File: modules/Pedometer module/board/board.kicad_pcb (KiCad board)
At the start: 2 copper layers, 54 parts, among them IC1 DW01A, J1 USB_C_Receptacle, J2 Conn_02x12_Odd_Even, J3 Conn_01x06_Female, J4 Conn_01x08_Female, J5 Conn_01x02_Female, Q1 AO3400A, Q2 AO3401A, Q3 FS8205A, SW1 SW_Push, SW2 SW_Push, U1 HT7833, U2 ESP32-WROOM-32D, U3 ADXL345BCCZ, U4 TP4056

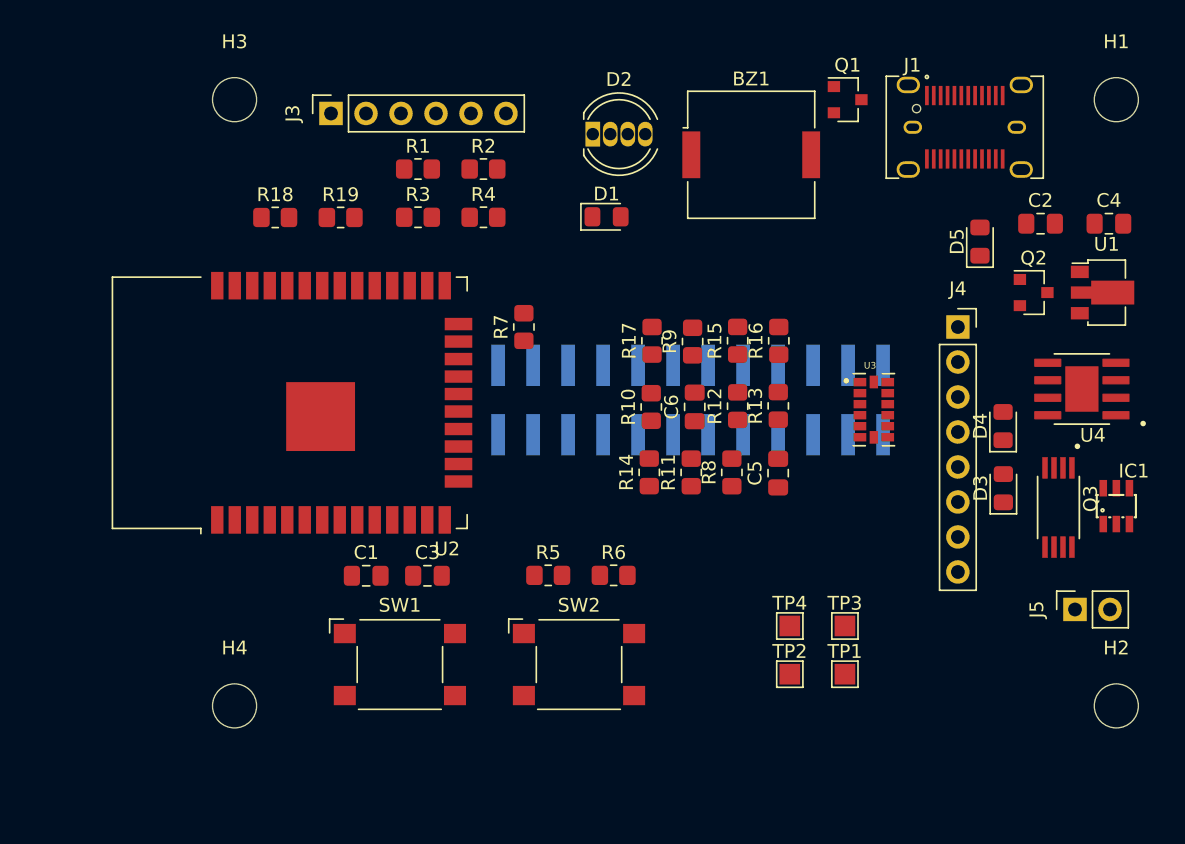
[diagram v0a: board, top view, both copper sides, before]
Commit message: Pedometer module: Schematic and PCB layout
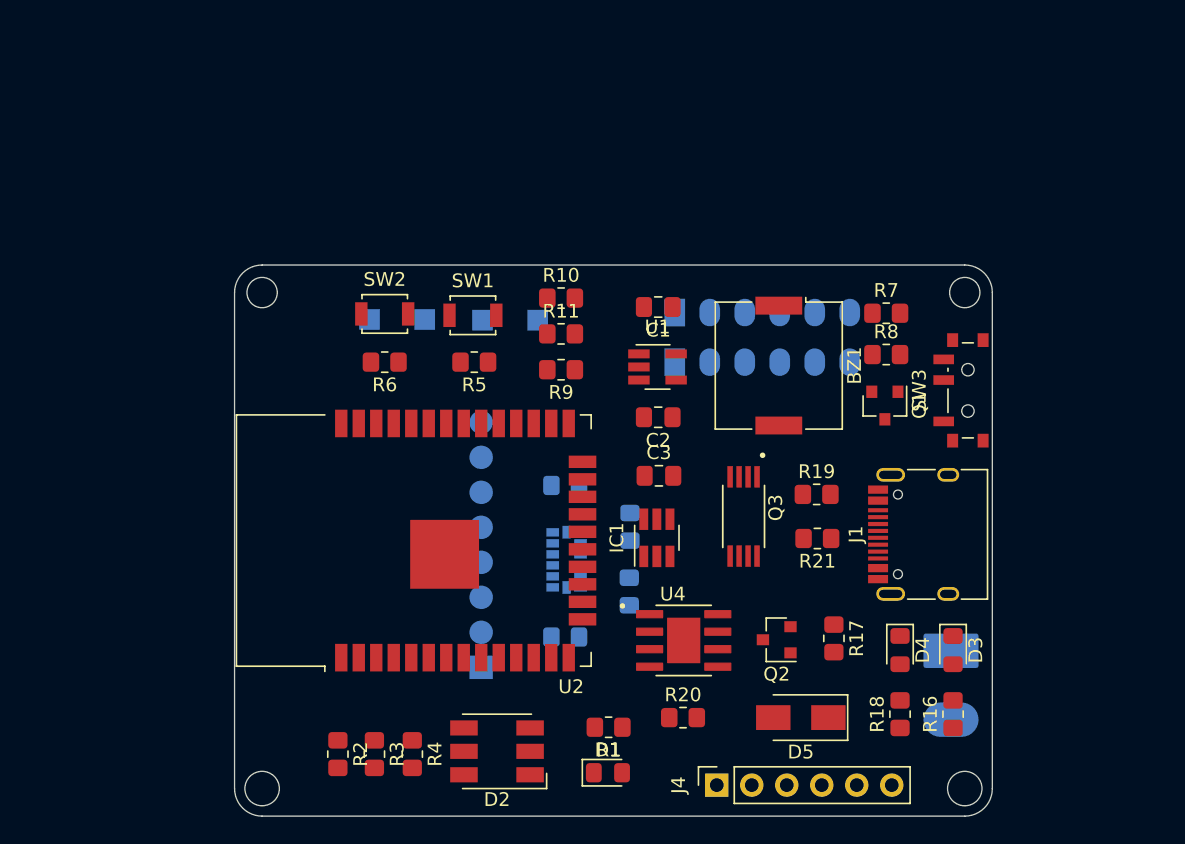
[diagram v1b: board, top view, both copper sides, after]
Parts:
- removed the C1 at (127.6, 112.6)
- removed the C3 at (132.0, 112.6)
- removed C6: 10uF, Capacitor_SMD:C_0805_2012Metric_Pad1.18x1.45mm_HandSolder
- added J3: Conn_01x06_Female, Board:SolderWire_1x06_P2.54mm, B.Cu at (149.9, 97.0)
- added R7: 100R, Resistor_SMD:R_0805_2012Metric_Pad1.20x1.40mm_HandSolder, F.Cu at (165.3, 93.5)
- added R8: 10k, Resistor_SMD:R_0805_2012Metric_Pad1.20x1.40mm_HandSolder, F.Cu at (165.3, 96.5)
- added SW3: SW_SPST, Board:SW-SPDT-PCM12, F.Cu at (170.9, 99.1)
- C1: renamed from C2; value 1uF -> 10uF
- C2: renamed from C4; value 2.2uF -> 10uF
- D2: value LED_RGBC -> LED_RGB; footprint LED_THT:LED_D5.0mm-4_RGB -> LED_SMD:LED_RGB_5050-6
- D5: footprint Diode_SMD:D_0805_2012Metric_Pad1.15x1.40mm_HandSolder -> Diode_SMD:D_SMA
- H1, H2: footprint MountingHole:MountingHole_3.2mm_M3 -> MountingHole:MountingHole_2.2mm_M2
- H3, H4: footprint MountingHole:MountingHole_3.2mm_M3 -> MountingHole:MountingHole_2.5mm
- IC1: footprint board:SOT23-6 -> Package_TO_SOT_SMD:SOT-23-6_Handsoldering
- J1: value USB_C_Receptacle -> USB_C_Receptacle_USB2.0; footprint Connector_USB:USB_C_Receptacle_JAE_DX07S024WJ1R350 -> Connector_USB:USB_C_Receptacle_HRO_TYPE-C-31-M-12
- J2: value Conn_02x12_Odd_Even -> Conn_01x06_Female; footprint Connector_PinSocket_2.54mm:PinSocket_2x12_P2.54mm_Vertical_SMD -> Board:SolderWire_1x06_P2.54mm
- J5: renamed from J4; footprint Connector_PinSocket_2.54mm:PinSocket_1x08_P2.54mm_Vertical -> Board:ADXL345_Breakout; moved to B.Cu
- J6: renamed from J5; footprint Connector_PinSocket_2.54mm:PinSocket_1x02_P2.54mm_Vertical -> Board:SolderWire-SMD-BATT; moved to B.Cu
- Q3: footprint board:SOP65P640X120-8N -> Board:SOP65P640X120-8N
- R12: renamed from R8; moved to B.Cu
- R13: renamed from R9; moved to B.Cu
- R14: renamed from R10; moved to B.Cu
- R15: renamed from R11; moved to B.Cu
- SW1, SW2: footprint Button_Switch_SMD:SW_SPST_Omron_B3FS-100xP -> Button_Switch_SMD:SW_SPST_B3U-1000P
- TP1, TP2, TP3, TP4, U3: moved to B.Cu
- U1: value HT7833 -> ME6211; footprint Package_TO_SOT_SMD:SOT-89-3 -> Package_TO_SOT_SMD:SOT-23-5_HandSoldering
- U4: footprint board:SOP127P600X175-9N -> Board:SOP127P600X175-9N
- moved H2 68.9 mm to (120.0, 92.0)
- moved J4 56.2 mm to (153.0, 127.8)
- moved H4 53.3 mm to (171.0, 128.0)
- moved H3 50.0 mm to (120.0, 128.0)
- moved D2 45.3 mm to (137.1, 125.3), turned to 180 degrees
- moved R2 43.8 mm to (125.5, 125.5), turned to 270 degrees
- moved R1 42.8 mm to (145.2, 123.5), turned to 180 degrees
- moved J5 42.3 mm to (136.0, 119.0)
- moved D1 40.4 mm to (145.1, 126.8)
- moved TP2 39.9 mm to (127.8, 94.0)
- moved TP1 39.9 mm to (131.8, 94.0)
- moved R4 39.3 mm to (130.9, 125.5), turned to 270 degrees
- moved R3 39.1 mm to (128.2, 125.5), turned to 270 degrees
- moved D5 36.9 mm to (159.1, 122.8), turned to 180 degrees
- moved C2 35.6 mm to (148.8, 101.0), turned to 180 degrees
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- renumbered C5 to C3, J3 to J4, R18 to R10, R19 to R11, R12 to R16, R13 to R17, R14 to R18, R15 to R19, R16 to R20, R17 to R21, R7 to R9
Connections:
- C1 pad 2: Net-(C2-Pad2) -> GND
- C2 pad 2: Net-(C2-Pad2) -> GND
- D2 pad 1: Net-(D2-Pad1) -> GND
- D2 pad 2: Net-(D2-Pad2) -> GND
- D2 pad 3: Net-(D2-Pad3) -> GND
- D2 pad 4: GND -> Net-(D2-Pad4)
- J2 pad 1: +5V -> /IO35
- J2 pad 2: +3V3 -> /IO34
- J2 pad 3: GND -> /IO33
- J2 pad 4: GND -> /IO32
- J2 pad 5: /IO21 -> /IO27
- J2 pad 6: /IO4 -> /IO5
- Q1 pad 1: /BUZZER -> Net-(Q1-Pad1)
- R2 pad 1: Net-(D2-Pad3) -> Net-(D2-Pad4)
- R2 pad 2: /IO27 -> /IO26
- R3 pad 1: Net-(D2-Pad2) -> Net-(D2-Pad5)
- R3 pad 2: /IO26 -> /IO25
- R4 pad 1: Net-(D2-Pad1) -> Net-(D2-Pad6)
- R4 pad 2: /IO25 -> /IO23
- U1 pad 1: GND -> VCC
- U1 pad 2: VCC -> GND
- U1 pad 3: +3V3 -> VCC
- U2 pad 23: /IO15 -> (no net)
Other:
- board outline added: 55 x 40 mm

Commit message: Pedometer module: PCB size reduced
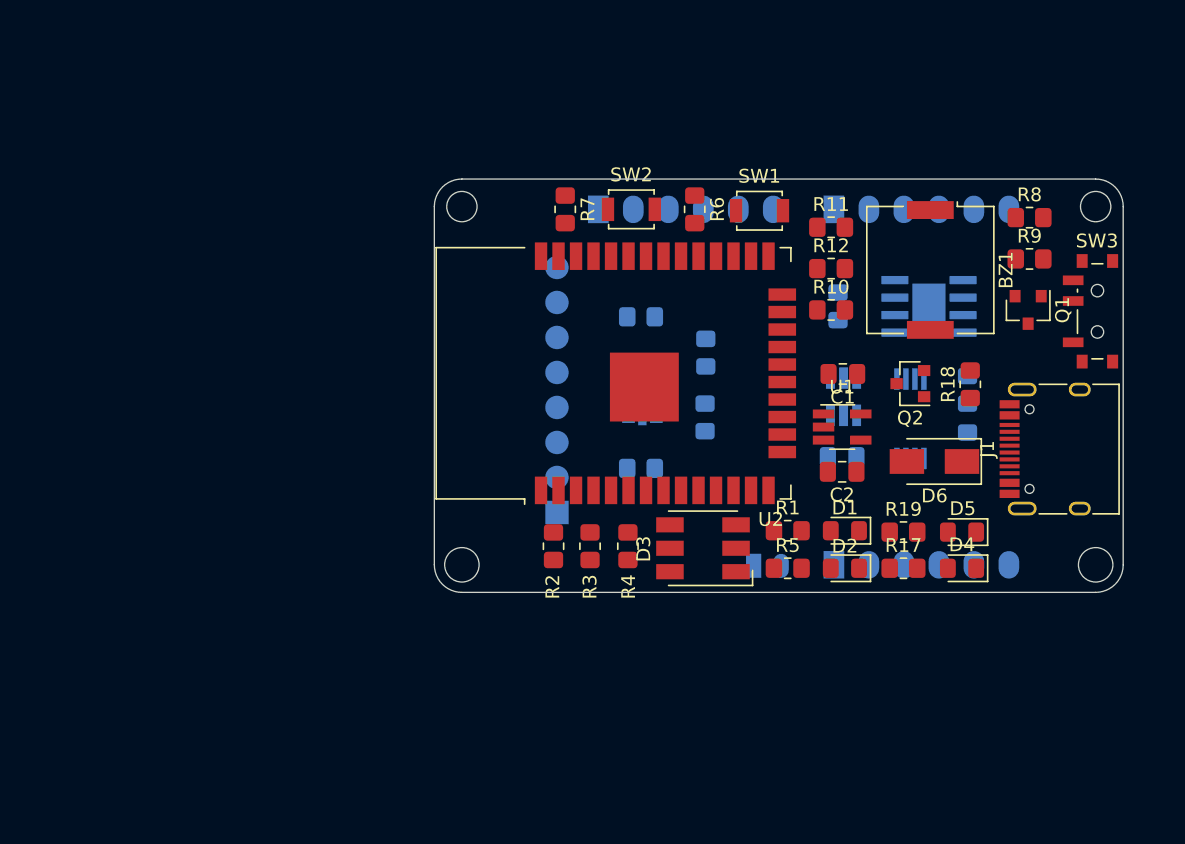
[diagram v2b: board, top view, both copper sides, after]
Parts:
- removed TP1, TP2, TP3, TP4: TestPoint, TestPoint:TestPoint_Pad_1.5x1.5mm
- added D2: LED, LED_SMD:LED_0805_2012Metric_Pad1.15x1.40mm_HandSolder, F.Cu at (162.3, 112.0)
- added R5: 12k, Resistor_SMD:R_0805_2012Metric_Pad1.20x1.40mm_HandSolder, F.Cu at (158.2, 112.0)
- C3, IC1, Q3, U4: moved to B.Cu
- J4: footprint Connector_PinSocket_2.54mm:PinSocket_1x06_P2.54mm_Vertical -> Board:SolderWire_1x06_P2.54mm; moved to B.Cu
- J6: footprint Board:SolderWire-SMD-BATT -> Board:SolderWire_1x02_P2.00mm
- R20: renamed from R19; moved to B.Cu
- R21: renamed from R20; moved to B.Cu
- R22: renamed from R21; moved to B.Cu
- moved J4 42.7 mm to (144.4, 86.0), turned to 270 degrees
- moved R21 31.9 mm to (161.8, 93.0), turned to 90 degrees
- moved U4 30.1 mm to (168.4, 93.0)
- moved D1 24.6 mm to (162.3, 109.3), turned to 180 degrees
- moved SW1 22.1 mm to (156.1, 86.1)
- moved H3 21.8 mm to (134.5, 111.8)
- moved R2 21.7 mm to (141.2, 110.4)
- moved R3 21.7 mm to (143.8, 110.4)
- moved R4 21.7 mm to (146.6, 110.4)
- moved D3 21.0 mm to (152.0, 110.6)
- moved Q2 21.0 mm to (167.1, 98.6)
- moved D6 21.0 mm to (168.8, 104.3)
- moved R18 20.9 mm to (171.4, 98.7)
- moved R11 20.3 mm to (161.3, 87.3)
- moved R12 20.2 mm to (161.3, 90.3)
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- renumbered D2 to D3, D3 to D4, D4 to D5, D5 to D6, R9 to R10, R10 to R11, R11 to R12, R12 to R13, R13 to R14, R14 to R15, R15 to R16, R16 to R17, R17 to R18, R18 to R19, R5 to R6, R6 to R7, R7 to R8, R8 to R9
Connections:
- R9 pad 2: Net-(BZ1-Pad1) -> GND
- U2 pad 23: (no net) -> /IO15
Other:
- board size 55 x 40 mm -> 50 x 30 mm

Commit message: Pedometer module: PCB complete
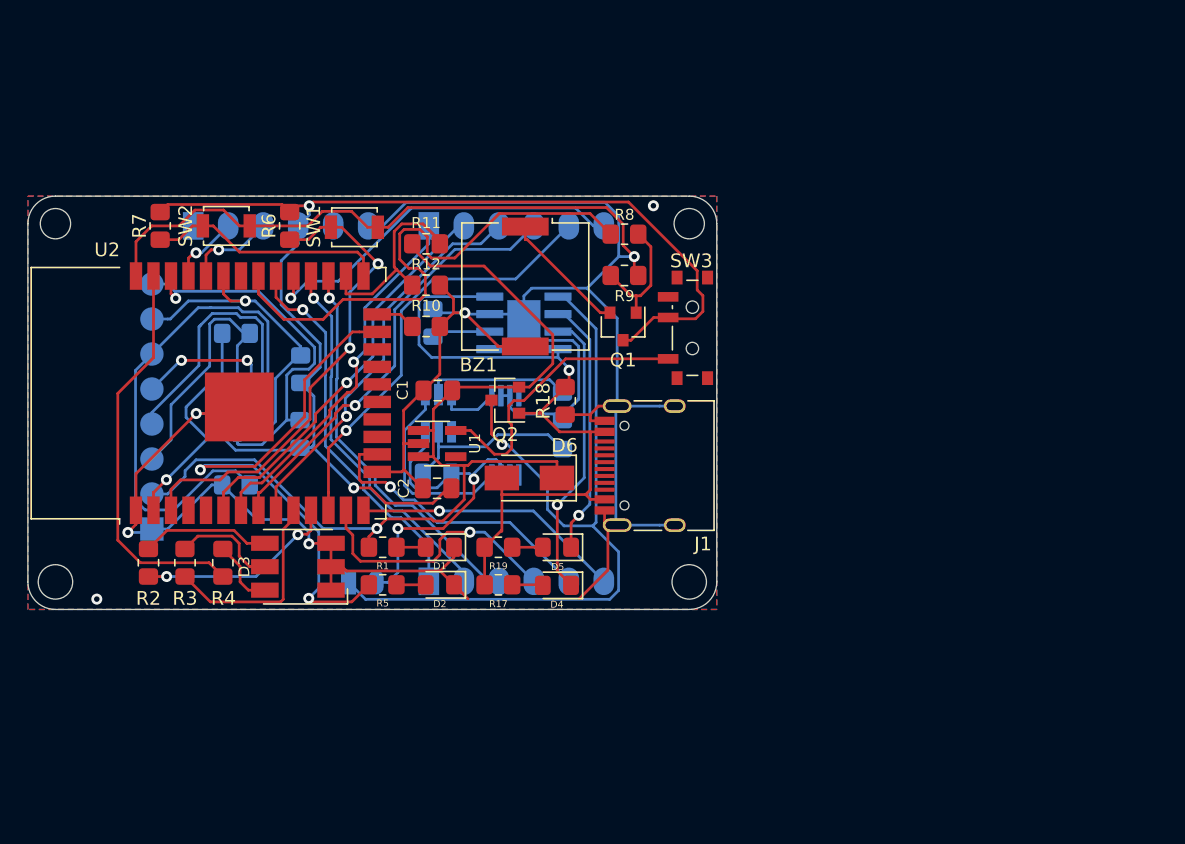
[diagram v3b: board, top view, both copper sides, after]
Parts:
- U2: footprint RF_Module:ESP32-WROOM-32 -> Board:ESP32-WROOM-32
- moved H1 29.5 mm to (151.0, 87.0)
- moved H2 29.5 mm to (105.0, 87.0)
- moved H3 29.5 mm to (105.0, 113.0)
- moved H4 29.5 mm to (151.0, 113.0)
- moved U2 29.4 mm to (119.1, 99.3)
- moved D3 29.4 mm to (122.6, 111.9)
- moved D4 29.4 mm to (141.4, 113.2)
- moved BZ1 29.4 mm to (139.1, 91.6)
- moved C1 29.4 mm to (132.8, 99.1)
- moved C2 29.4 mm to (132.7, 106.2)
- moved C3 29.4 mm to (132.7, 105.1)
- moved D1 29.4 mm to (132.9, 110.5)
- moved D2 29.4 mm to (132.9, 113.2)
- moved D6 29.4 mm to (139.4, 105.5)
- moved J1 29.4 mm to (148.9, 104.6)
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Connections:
- net /IO21 renamed /SDA
- net /IO22 renamed /SCL
- net /IO23 renamed /LED-R
- net /IO25 renamed /LED-G
- net /IO26 renamed /LED-B
- J5 pad 2: +3V3 -> VCC
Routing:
- net GND: track 0.00 -> 226.1 mm, vias 0 -> 7
- net +3V3: track 0.00 -> 109.9 mm, vias 0 -> 3
- net VCC: track 0.00 -> 72.5 mm, vias 0 -> 1
- net /BMS/BATT+: track 0.00 -> 59.0 mm, vias 0 -> 1
- net +5V: track 0.00 -> 52.1 mm, vias 0 -> 1
- net /IMU/SDO: track 0.00 -> 40.0 mm
- net /BUZZER: track 0.00 -> 39.5 mm
- net /IO15: track 0.00 -> 39.4 mm, vias 0 -> 2
- net /EN: track 0.00 -> 34.9 mm, vias 0 -> 2
- net /IO32: track 0.00 -> 31.9 mm, vias 0 -> 1
- net /IO27: track 0.00 -> 31.4 mm, vias 0 -> 1
- net /IO34: track 0.00 -> 29.0 mm, vias 0 -> 1
- net /LED-R: track 0.00 -> 29.0 mm
- net /SCL: track 0.00 -> 28.7 mm, vias 0 -> 1
- net /IO33: track 0.00 -> 28.6 mm, vias 0 -> 1
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- added copper zone on B.Cu, net GND
- added copper zone on F.Cu, net GND
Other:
- net class Default: trace_width 0.25 -> 0.2

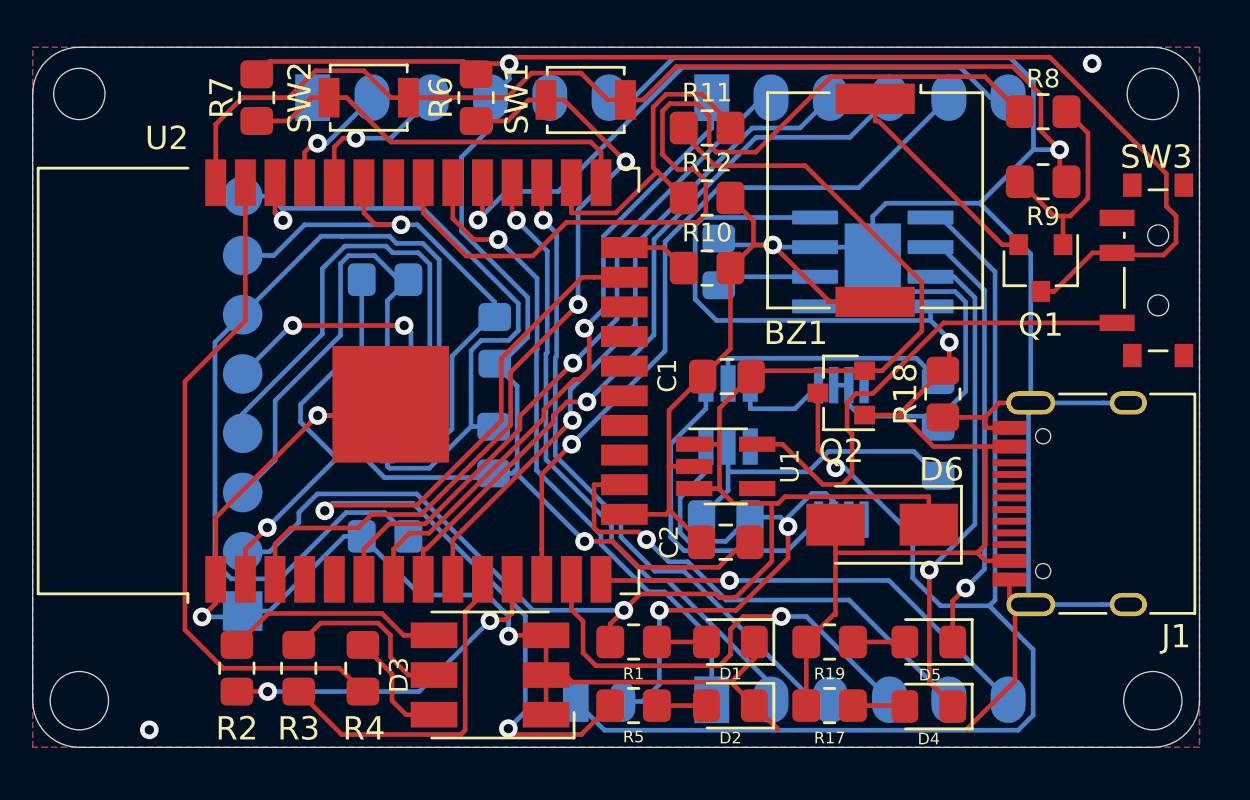
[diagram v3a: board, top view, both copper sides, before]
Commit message: Pedometer module: PCB modular
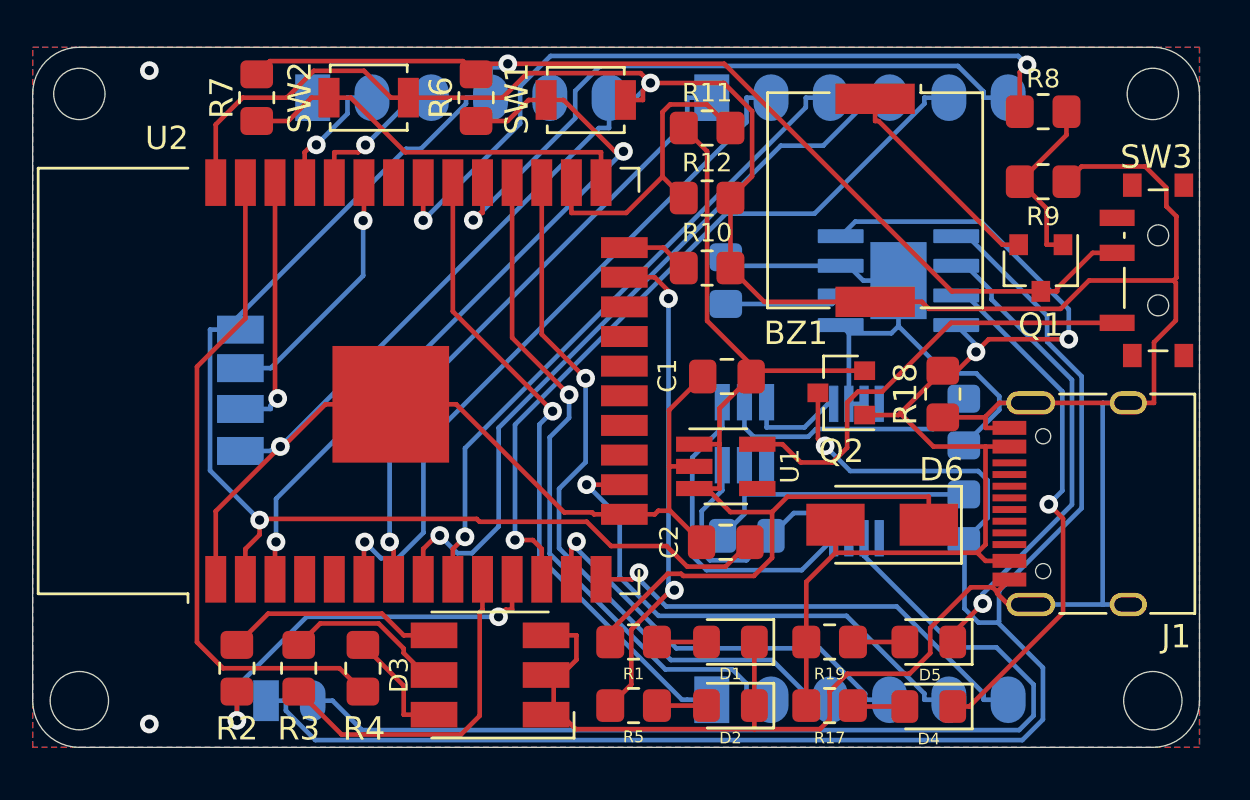
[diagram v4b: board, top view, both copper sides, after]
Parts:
- removed J5: Conn_01x08_Female, Board:ADXL345_Breakout
- removed R13, R14, R15, R16: 4.7k, Resistor_SMD:R_0805_2012Metric_Pad1.20x1.40mm_HandSolder
- U3: value ADXL345BCCZ -> Inertial_Measurement_Unit; footprint board:PQFN80P300X500X100-14N -> Board:Inertial_Measurement_Unit_Board
- moved J6 13.3 mm to (113.0, 113.0)
- moved U3 1.42 mm to (119.4, 99.6)
- moved R20 1.36 mm to (142.9, 105.2)
- moved R22 1.36 mm to (142.9, 101.1)
- moved U4 1.36 mm to (140.1, 95.0)
- moved C3 1.20 mm to (133.6, 105.9)
- moved IC1 1.06 mm to (133.5, 101.6)
- moved Q3 1.03 mm to (138.3, 103.2)
- moved R21 0.85 mm to (132.7, 95.0)
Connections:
- U3 pad 2: GND -> /SDA
- U3 pad 3: (no net) -> /SCL
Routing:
- net /IMU/SDO: track 40.0 -> 0.00 mm
- net /BMS/BATT-: track 26.6 -> 56.2 mm, vias 2 -> 0
- net VCC: track 72.5 -> 46.3 mm, vias 1 -> 0
- net /IMU/INT1: track 20.3 -> 0.00 mm
- net /BMS/BATT+: track 59.0 -> 77.7 mm
- net /IMU/CS: track 18.7 -> 0.00 mm
- net /IO15: track 39.4 -> 21.2 mm
- net /SCL: track 28.7 -> 11.2 mm
- net +3V3: track 109.9 -> 95.5 mm, vias 3 -> 2
- net /SDA: track 24.3 -> 10.9 mm
- net /IMU/INT2: track 9.34 -> 0.00 mm, vias 2 -> 0
- net GND: track 226.1 -> 218.1 mm, vias 7 -> 4
- net /BUZZER: track 39.5 -> 33.6 mm, vias 0 -> 2
- net /IO16: track 28.5 -> 31.4 mm
- net /EN: track 34.9 -> 32.1 mm
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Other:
- board text added: "InputBlackBoxOutput"
